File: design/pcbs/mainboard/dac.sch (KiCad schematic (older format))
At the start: 22 parts, among them U10 TPS7A49, U11 PCM1792A

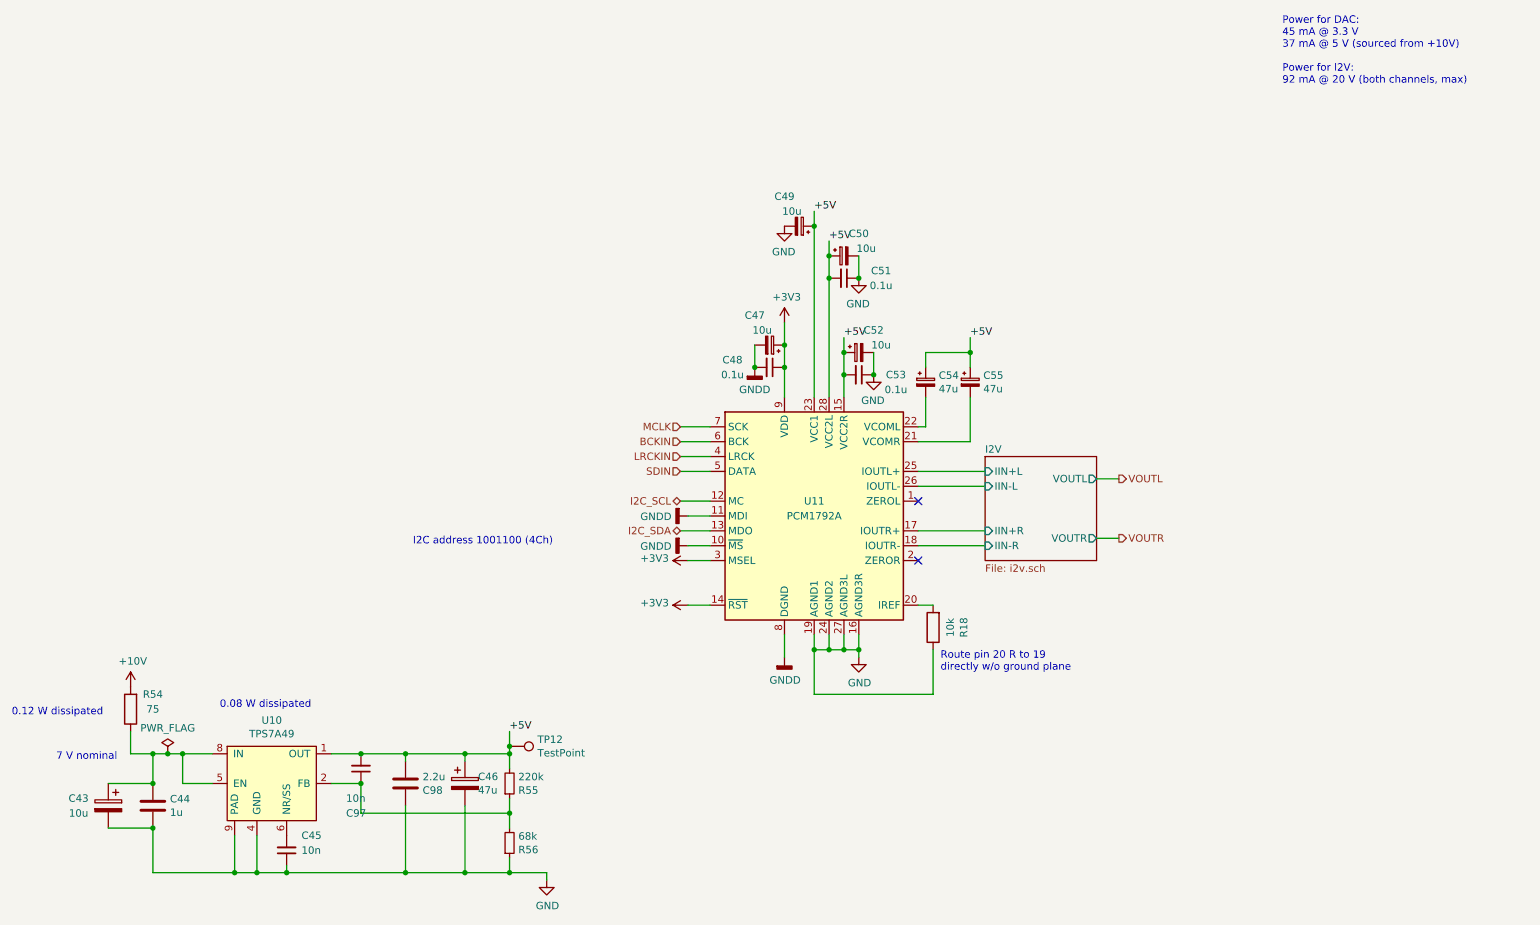
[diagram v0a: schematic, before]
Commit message: Renumbered footprints to follow board position.
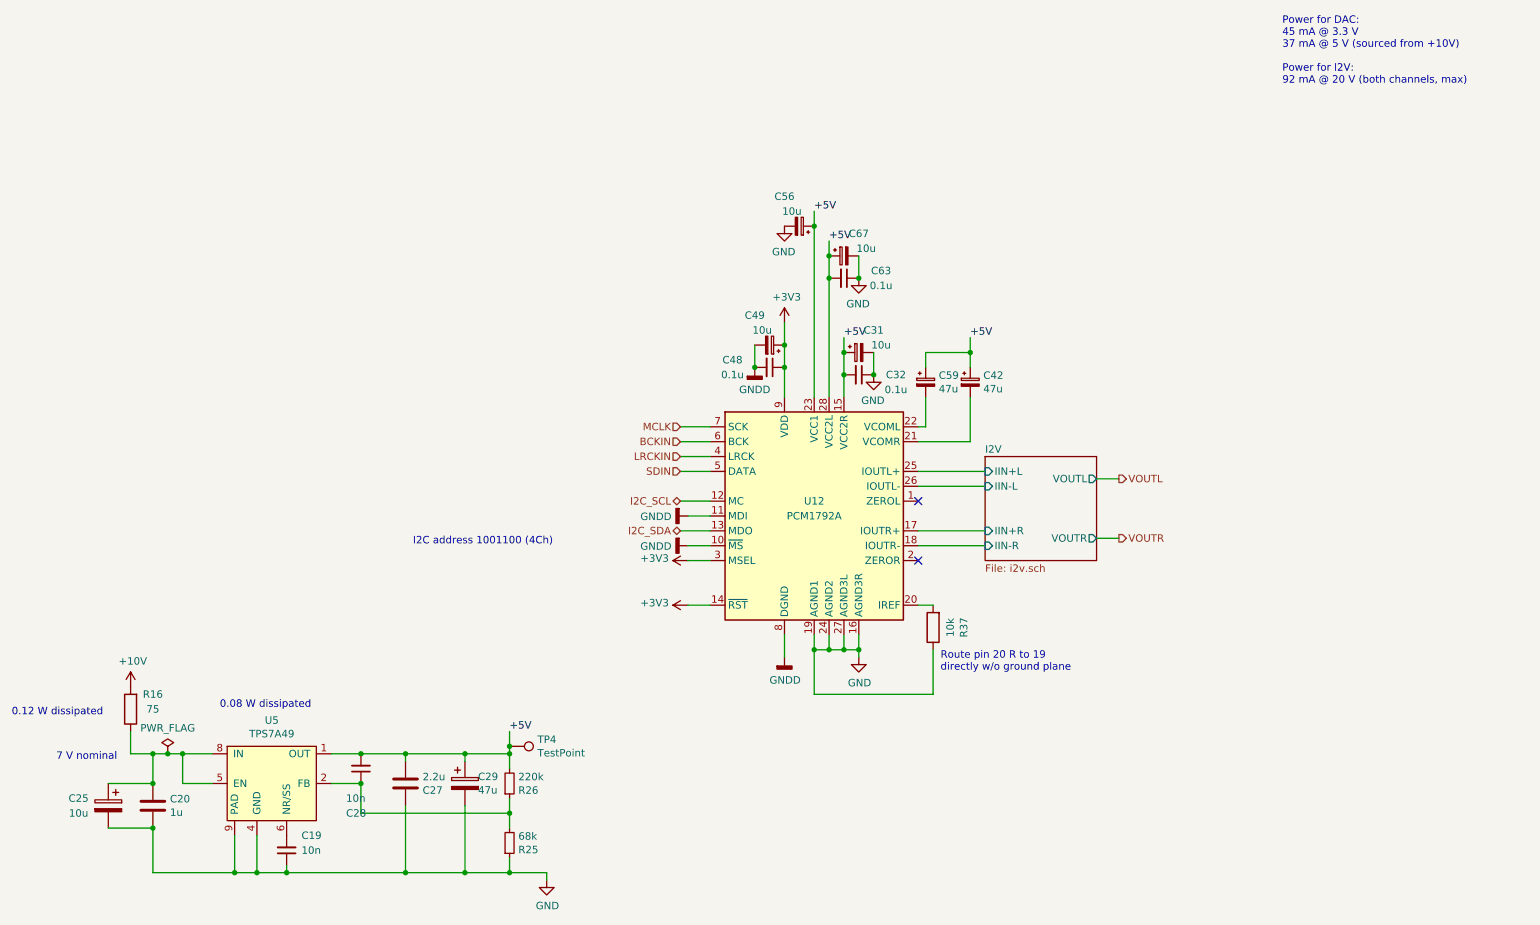
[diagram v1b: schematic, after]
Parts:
- renumbered C45 to C19, C44 to C20, C43 to C25, C98 to C27, C97 to C28, C46 to C29, C52 to C31, C53 to C32, C55 to C42, C47 to C49, C49 to C56, C54 to C59, C51 to C63, C50 to C67, R54 to R16, R56 to R25, R55 to R26, R18 to R37, TP12 to TP4, U11 to U12, U10 to U5
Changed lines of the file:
@@
 +5V
 $Comp
-L Device:C C44
+L Device:C C20
 U 1 1 5ECA0FE5
 P 2000 5900
-F 0 "C44" H 2115 5946 50  0000 L CNN
+F 0 "C20" H 2115 5946 50  0000 L CNN
 F 1 "1u" H 2115 5855 50  0000 L CNN
 F 2 "Capacitor_SMD:C_0805_2012Metric" H 2038 5750 50  0001 C CNN
@@
 	7250 4550 7150 4550
 $Comp
-L Device:R R18
+L Device:R R37
 U 1 1 5EC96EB0
 P 7250 4700
-F 0 "R18" V 7043 4700 50  0000 C CNN
+F 0 "R37" V 7043 4700 50  0000 C CNN
 F 1 "10k" V 7134 4700 50  0000 C CNN
 F 2 "Resistor_SMD:R_0402_1005Metric" V 7180 4700 50  0001 C CNN
@@
 	7200 3150 7200 3350
 $Comp
-L Audio:PCM1792A U11
+L Audio:PCM1792A U12
 U 1 1 5EC79C7B
 P 6450 3950
-F 0 "U11" H 6450 4050 50  0000 C CNN
+F 0 "U12" H 6450 4050 50  0000 C CNN
 F 1 "PCM1792A" H 6450 3950 50  0000 C CNN
 F 2 "Package_SO:SSOP-28_5.3x10.2mm_P0.65mm" H 6450 3950 50  0001 C CNN
@@
 Connection ~ 6650 3000
 $Comp
-L Device:C_Small C53
+L Device:C_Small C32
 U 1 1 5EC8EDB7
 P 6750 3000
-F 0 "C53" V 6750 3250 50  0000 C CNN
+F 0 "C32" V 6750 3250 50  0000 C CNN
 F 1 "0.1u" V 6850 3250 50  0000 C CNN
 F 2 "Capacitor_SMD:C_0603_1608Metric" H 6788 2850 50  0001 C CNN
@@
 Connection ~ 6550 2350
 $Comp
-L Device:C_Small C51
+L Device:C_Small C63
 U 1 1 5EC8BFA6
 P 6650 2350
-F 0 "C51" V 6600 2600 50  0000 C CNN
+F 0 "C63" V 6600 2600 50  0000 C CNN
 F 1 "0.1u" V 6700 2600 50  0000 C CNN
 F 2 "Capacitor_SMD:C_0603_1608Metric" H 6688 2200 50  0001 C CNN
@@
 $EndComp
 $Comp
-L Device:CP_Small C55
+L Device:CP_Small C42
 U 1 1 5EC776CB
 P 7500 3050
-F 0 "C55" H 7588 3096 50  0000 L CNN
+F 0 "C42" H 7588 3096 50  0000 L CNN
 F 1 "47u" H 7588 3005 50  0000 L CNN
 F 2 "Capacitor_THT:CP_Radial_D5.0mm_P2.00mm" H 7538 2900 50  0001 C CNN
@@
 $EndComp
 $Comp
-L Device:CP_Small C54
+L Device:CP_Small C59
 U 1 1 5EC768A9
 P 7200 3050
-F 0 "C54" H 7288 3096 50  0000 L CNN
+F 0 "C59" H 7288 3096 50  0000 L CNN
 F 1 "47u" H 7288 3005 50  0000 L CNN
 F 2 "Capacitor_THT:CP_Radial_D5.0mm_P2.00mm" H 7238 2900 50  0001 C CNN
@@
 P 6650 2200
 AR Path="/5EC77FFA/5ECF2F54" Ref="C?"  Part="1"
-AR Path="/5EC7811C/5ECF2F54" Ref="C50"  Part="1"
-F 0 "C50" V 6500 2100 50  0000 C CNN
+AR Path="/5EC7811C/5ECF2F54" Ref="C67"  Part="1"
+F 0 "C67" V 6500 2100 50  0000 C CNN
 F 1 "10u" V 6600 2050 50  0000 C CNN
 F 2 "Capacitor_Tantalum_SMD:CP_EIA-3216-18_Kemet-A" H 6688 2050 50  0001 C CNN
@@
 P 6350 2000
 AR Path="/5EC77FFA/5ECF477A" Ref="C?"  Part="1"
-AR Path="/5EC7811C/5ECF477A" Ref="C49"  Part="1"
-F 0 "C49" V 6550 1900 50  0000 C CNN
+AR Path="/5EC7811C/5ECF477A" Ref="C56"  Part="1"
+F 0 "C56" V 6550 1900 50  0000 C CNN
 F 1 "10u" V 6450 1950 50  0000 C CNN
 F 2 "Capacitor_Tantalum_SMD:CP_EIA-3216-18_Kemet-A" H 6388 1850 50  0001 C CNN
@@
 P 6150 2800
 AR Path="/5EC77FFA/5ECF5115" Ref="C?"  Part="1"
-AR Path="/5EC7811C/5ECF5115" Ref="C47"  Part="1"
-F 0 "C47" V 6350 2700 50  0000 C CNN
+AR Path="/5EC7811C/5ECF5115" Ref="C49"  Part="1"
+F 0 "C49" V 6350 2700 50  0000 C CNN
 F 1 "10u" V 6250 2750 50  0000 C CNN
 F 2 "Capacitor_Tantalum_SMD:CP_EIA-3216-18_Kemet-A" H 6188 2650 50  0001 C CNN
@@
 P 6750 2850
 AR Path="/5EC77FFA/5ECF5A07" Ref="C?"  Part="1"
-AR Path="/5EC7811C/5ECF5A07" Ref="C52"  Part="1"
-F 0 "C52" V 6600 2750 50  0000 C CNN
+AR Path="/5EC7811C/5ECF5A07" Ref="C31"  Part="1"
+F 0 "C31" V 6600 2750 50  0000 C CNN
 F 1 "10u" V 6700 2700 50  0000 C CNN
 F 2 "Capacitor_Tantalum_SMD:CP_EIA-3216-18_Kemet-A" H 6788 2700 50  0001 C CNN
@@
 P 1700 5900
 AR Path="/5EC77FFA/5ECD8C25" Ref="C?"  Part="1"
-AR Path="/5EC7811C/5ECD8C25" Ref="C43"  Part="1"
-F 0 "C43" H 1900 5950 50  0000 C CNN
+AR Path="/5EC7811C/5ECD8C25" Ref="C25"  Part="1"
+F 0 "C25" H 1900 5950 50  0000 C CNN
 F 1 "10u" H 1900 5850 50  0000 C CNN
 F 2 "Capacitor_Tantalum_SMD:CP_EIA-3216-18_Kemet-A" H 1738 5750 50  0001 C CNN
@@
 NoConn ~ 7150 4250
 $Comp
-L Connector:TestPoint TP12
+L Connector:TestPoint TP4
 U 1 1 5EE7E152
 P 4400 5500
-F 0 "TP12" V 4354 5688 50  0000 L CNN
+F 0 "TP4" V 4354 5688 50  0000 L CNN
 F 1 "TestPoint" V 4445 5688 50  0000 L CNN
 F 2 "TestPoint:TestPoint_THTPad_D3.0mm_Drill1.5mm" H 4600 5500 50  0001 C CNN
@@
 	6250 4750 6250 4900
 $Comp
-L Device:R R54
+L Device:R R16
 U 1 1 5EE0ACD0
 P 1850 5250
-F 0 "R54" H 1700 5150 50  0000 C CNN
+F 0 "R16" H 1700 5150 50  0000 C CNN
 F 1 "75" H 1700 5250 50  0000 C CNN
 F 2 "Resistor_SMD:R_1206_3216Metric" V 1780 5250 50  0001 C CNN
@@
 P 3400 5650
 AR Path="/5EC7824B/5EE227BA" Ref="C?"  Part="1"
-AR Path="/5EC7811C/5EE227BA" Ref="C97"  Part="1"
-F 0 "C97" H 3300 5950 50  0000 L CNN
+AR Path="/5EC7811C/5EE227BA" Ref="C28"  Part="1"
+F 0 "C28" H 3300 5950 50  0000 L CNN
 F 1 "10n" H 3300 5850 50  0000 L CNN
 F 2 "Capacitor_SMD:C_0603_1608Metric" H 3438 5500 50  0001 C CNN
@@
 P 2900 6200
 AR Path="/5EC7824B/5EE227C6" Ref="C?"  Part="1"
-AR Path="/5EC7811C/5EE227C6" Ref="C45"  Part="1"
-F 0 "C45" H 3000 6100 50  0000 L CNN
+AR Path="/5EC7811C/5EE227C6" Ref="C19"  Part="1"
+F 0 "C19" H 3000 6100 50  0000 L CNN
 F 1 "10n" H 3000 6200 50  0000 L CNN
 F 2 "Capacitor_SMD:C_0603_1608Metric" H 2938 6050 50  0001 C CNN
@@
 P 4400 5750
 AR Path="/5EC7824B/5EE227CF" Ref="R?"  Part="1"
-AR Path="/5EC7811C/5EE227CF" Ref="R55"  Part="1"
-F 0 "R55" H 4459 5796 50  0000 L CNN
+AR Path="/5EC7811C/5EE227CF" Ref="R26"  Part="1"
+F 0 "R26" H 4459 5796 50  0000 L CNN
 F 1 "220k" H 4459 5705 50  0000 L CNN
 F 2 "Resistor_SMD:R_0402_1005Metric" H 4400 5750 50  0001 C CNN
@@
 P 4400 6150
 AR Path="/5EC7824B/5EE227ED" Ref="R?"  Part="1"
-AR Path="/5EC7811C/5EE227ED" Ref="R56"  Part="1"
-F 0 "R56" H 4459 6196 50  0000 L CNN
+AR Path="/5EC7811C/5EE227ED" Ref="R25"  Part="1"
+F 0 "R25" H 4459 6196 50  0000 L CNN
 F 1 "68k" H 4459 6105 50  0000 L CNN
 F 2 "Resistor_SMD:R_0402_1005Metric" H 4400 6150 50  0001 C CNN
@@
 P 2800 5750
 AR Path="/5EC7824B/5EE227AD" Ref="U?"  Part="1"
-AR Path="/5EC7811C/5EE227AD" Ref="U10"  Part="1"
-F 0 "U10" H 2800 6175 50  0000 C CNN
+AR Path="/5EC7811C/5EE227AD" Ref="U5"  Part="1"
+F 0 "U5" H 2800 6175 50  0000 C CNN
 F 1 "TPS7A49" H 2800 6084 50  0000 C CNN
 F 2 "Package_SO:MSOP-8-1EP_3x3mm_P0.65mm_EP1.68x1.88mm_ThermalVias" H 2750 5750 50  0001 C CNN
@@
 	1850 5400 1850 5550
 $Comp
-L Device:CP C46
+L Device:CP C29
 U 1 1 5EDC1BA1
 P 4100 5750
-F 0 "C46" H 4188 5796 50  0000 L CNN
+F 0 "C29" H 4188 5796 50  0000 L CNN
 F 1 "47u" H 4188 5705 50  0000 L CNN
 F 2 "Capacitor_THT:CP_Radial_D5.0mm_P2.00mm" H 4138 5600 50  0001 C CNN
@@
 P 3700 5750
 AR Path="/5EC7824B/5EE22817" Ref="C?"  Part="1"
-AR Path="/5EC7811C/5EE22817" Ref="C98"  Part="1"
-F 0 "C98" H 3815 5796 50  0000 L CNN
+AR Path="/5EC7811C/5EE22817" Ref="C27"  Part="1"
+F 0 "C27" H 3815 5796 50  0000 L CNN
 F 1 "2.2u" H 3815 5705 50  0000 L CNN
 F 2 "Capacitor_SMD:C_1206_3216Metric" H 3738 5600 50  0001 C CNN

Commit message: Fixed title blocks. Added fab outputs.
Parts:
- U5: LCSC (none) -> C16430
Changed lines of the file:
@@
 encoding utf-8
 Sheet 6 10
-Title ""
-Date ""
-Rev ""
-Comp ""
-Comment1 ""
-Comment2 ""
+Title "DAC1 Main board"
+Date "2020-06-27"
+Rev "1.0.0"
+Comp "© Mark Pinese 2020"
+Comment1 "To view a copy of this license, visit https://creativecommons.org/licenses/by/4.0"
+Comment2 "This work is licensed under CC BY 4.0."
 Comment3 ""
 Comment4 ""
@@
 F 4 "296-27751-1-ND" H 2800 5750 50  0001 C CNN "DigiKey"
 F 5 "Yes" H 2800 5750 50  0001 C CNN "Done"
+F 6 "C16430" H 2800 5750 50  0001 C CNN "LCSC"
 	1    2800 5750
 	1    0    0    -1

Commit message: Misc updates
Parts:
- added FB3: Ferrite_Bead_Small, Resistor_SMD:R_0603_1608Metric_Pad1.05x0.95mm_HandSolder, symbol Device:Ferrite_Bead_Small
- C42, C59: footprint Capacitor_THT:CP_Radial_D5.0mm_P2.00mm -> Capacitor_THT:CP_Radial_D6.3mm_P2.50mm; DigiKey 732-9306-1-ND -> 493-15014-ND; Function Noise reduction -> (none)
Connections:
- net +3V3: now also FB3.1; no longer U12.9 (VDD)
- net GND: now also C48.2, C49.2, U12.8 (DGND)
- net GNDD: no longer C48.2, C49.2, U12.8 (DGND)
- new net: FB3.2, U12.9 (VDD)
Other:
- moved on the sheet: C48, C49
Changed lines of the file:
@@
 	0    1    1    0
 $EndComp
-Connection ~ 6050 2950
-Wire Wire Line
-	6050 2950 6050 2800
-Wire Wire Line
-	6250 2950 6250 3150
-Connection ~ 6250 2950
+Wire Wire Line
+	6050 2750 6050 2600
 Connection ~ 6750 2350
 Wire Wire Line
@@
 $EndComp
 $Comp
-L Device:CP_Small C42
-U 1 1 5EC776CB
-P 7500 3050
-F 0 "C42" H 7588 3096 50  0000 L CNN
-F 1 "47u" H 7588 3005 50  0000 L CNN
-F 2 "Capacitor_THT:CP_Radial_D5.0mm_P2.00mm" H 7538 2900 50  0001 C CNN
-F 3 "https://katalog.we-online.de/pbs/datasheet/860240272001.pdf" H 7500 3050 50  0001 C CNN
-F 4 "<= 5V" H 7500 3050 50  0001 C CNN "Vbias"
-F 5 "Noise reduction" H 7500 3050 50  0001 C CNN "Function"
-F 6 "732-9306-1-ND" H 7500 3050 50  0001 C CNN "DigiKey"
-F 7 "Yes" H 7500 3050 50  0001 C CNN "Done"
-	1    7500 3050
-	1    0    0    -1
-$EndComp
-$Comp
 L Device:CP_Small C59
 U 1 1 5EC768A9
@@
 F 0 "C59" H 7288 3096 50  0000 L CNN
 F 1 "47u" H 7288 3005 50  0000 L CNN
-F 2 "Capacitor_THT:CP_Radial_D5.0mm_P2.00mm" H 7238 2900 50  0001 C CNN
-F 3 "https://katalog.we-online.de/pbs/datasheet/860240272001.pdf" H 7200 3050 50  0001 C CNN
+F 2 "Capacitor_THT:CP_Radial_D6.3mm_P2.50mm" H 7238 2900 50  0001 C CNN
+F 3 "" H 7200 3050 50  0001 C CNN
 F 4 "<= 5V" H 7200 3050 50  0001 C CNN "Vbias"
-F 5 "Noise reduction" H 7200 3050 50  0001 C CNN "Function"
-F 6 "732-9306-1-ND" H 7200 3050 50  0001 C CNN "DigiKey"
+F 5 "" H 7200 3050 50  0001 C CNN "Function"
+F 6 "493-15014-ND" H 7200 3050 50  0001 C CNN "DigiKey"
 F 7 "Yes" H 7200 3050 50  0001 C CNN "Done"
 	1    7200 3050
@@
 $EndComp
 $Comp
-L power:GNDD #PWR069
-U 1 1 5EC7256D
-P 6050 2950
-F 0 "#PWR069" H 6050 2700 50  0001 C CNN
-F 1 "GNDD" H 6050 2800 50  0000 C CNN
-F 2 "" H 6050 2950 50  0001 C CNN
-F 3 "" H 6050 2950 50  0001 C CNN
-	1    6050 2950
-	1    0    0    -1
-$EndComp
-$Comp
 L Device:C_Small C48
 U 1 1 5EC6F4C3
-P 6150 2950
-F 0 "C48" V 6100 2700 50  0000 C CNN
-F 1 "0.1u" V 6200 2700 50  0000 C CNN
-F 2 "Capacitor_SMD:C_0603_1608Metric" H 6188 2800 50  0001 C CNN
-F 3 "https://datasheet.lcsc.com/szlcsc/YAGEO-CC0603KRX7R9BB104_C14663.pdf" H 6150 2950 50  0001 C CNN
-F 4 "C14663" H 6150 2950 50  0001 C CNN "LCSC"
-F 5 "3.3" V 6150 2950 50  0001 C CNN "Vbias"
-F 6 "Decoupling" H 6150 2950 50  0001 C CNN "Function"
-F 7 "Yes" H 6150 2950 50  0001 C CNN "Done"
-	1    6150 2950
+P 6150 2750
+F 0 "C48" V 6100 2500 50  0000 C CNN
+F 1 "0.1u" V 6200 2500 50  0000 C CNN
+F 2 "Capacitor_SMD:C_0603_1608Metric" H 6188 2600 50  0001 C CNN
+F 3 "https://datasheet.lcsc.com/szlcsc/YAGEO-CC0603KRX7R9BB104_C14663.pdf" H 6150 2750 50  0001 C CNN
+F 4 "C14663" H 6150 2750 50  0001 C CNN "LCSC"
+F 5 "3.3" V 6150 2750 50  0001 C CNN "Vbias"
+F 6 "Decoupling" H 6150 2750 50  0001 C CNN "Function"
+F 7 "Yes" H 6150 2750 50  0001 C CNN "Done"
+	1    6150 2750
 	0    1    1    0
 $EndComp
@@
 L power:+3V3 #PWR071
 U 1 1 5EC6E821
-P 6250 2650
-F 0 "#PWR071" H 6250 2500 50  0001 C CNN
-F 1 "+3V3" H 6265 2823 50  0000 C CNN
-F 2 "" H 6250 2650 50  0001 C CNN
-F 3 "" H 6250 2650 50  0001 C CNN
-	1    6250 2650
+P 6250 2450
+F 0 "#PWR071" H 6250 2300 50  0001 C CNN
+F 1 "+3V3" H 6265 2623 50  0000 C CNN
+F 2 "" H 6250 2450 50  0001 C CNN
+F 3 "" H 6250 2450 50  0001 C CNN
+	1    6250 2450
 	1    0    0    -1
 $EndComp
@@
 	0    1    1    0
 $EndComp
-$Comp
-L power:GNDD #PWR072
-U 1 1 5EC6BB00
-P 6250 4900
-F 0 "#PWR072" H 6250 4650 50  0001 C CNN
-F 1 "GNDD" H 6254 4745 50  0000 C CNN
-F 2 "" H 6250 4900 50  0001 C CNN
-F 3 "" H 6250 4900 50  0001 C CNN
-	1    6250 4900
-	1    0    0    -1
-$EndComp
 Wire Wire Line
 	5600 4250 5750 4250
@@
 	0    -1   -1   0
 $EndComp
-Wire Wire Line
-	5550 3350 5750 3350
-Wire Wire Line
-	5750 3650 5550 3650
-Wire Wire Line
-	5550 3550 5750 3550
-Wire Wire Line
-	5550 3450 5750 3450
-Text HLabel 5550 3350 0    50   Input ~ 0
-MCLK
-Text HLabel 5550 3550 0    50   Input ~ 0
-LRCKIN
-Text HLabel 5550 3450 0    50   Input ~ 0
-BCKIN
-Text HLabel 5550 3650 0    50   Input ~ 0
-SDIN
 Text HLabel 5550 4050 0    50   BiDi ~ 0
 I2C_SDA
@@
 	6450 1900 6450 2000
 Wire Wire Line
-	6250 2650 6250 2800
+	6250 2450 6250 2600
 $Comp
 L Device:CP_Small C?
@@
 L Device:CP_Small C?
 U 1 1 5ECF5115
-P 6150 2800
+P 6150 2600
 AR Path="/5EC77FFA/5ECF5115" Ref="C?"  Part="1"
 AR Path="/5EC7811C/5ECF5115" Ref="C49"  Part="1"
-F 0 "C49" V 6350 2700 50  0000 C CNN
-F 1 "10u" V 6250 2750 50  0000 C CNN
-F 2 "Capacitor_Tantalum_SMD:CP_EIA-3216-18_Kemet-A" H 6188 2650 50  0001 C CNN
-F 3 "https://datasheet.lcsc.com/szlcsc/AVX-TAJA106K016RNJ_C7171.pdf" H 6150 2800 50  0001 C CNN
-F 4 "3.3" V 6150 2800 50  0001 C CNN "Vbias"
-F 5 "Decoupling" H 6150 2800 50  0001 C CNN "Function"
-F 6 "" V 6150 2800 50  0001 C CNN "DigiKey"
-F 7 "C7171" H 6150 2800 50  0001 C CNN "LCSC"
-F 8 "Yes" H 6150 2800 50  0001 C CNN "Done"
-	1    6150 2800
+F 0 "C49" V 6350 2500 50  0000 C CNN
+F 1 "10u" V 6250 2550 50  0000 C CNN
+F 2 "Capacitor_Tantalum_SMD:CP_EIA-3216-18_Kemet-A" H 6188 2450 50  0001 C CNN
+F 3 "https://datasheet.lcsc.com/szlcsc/AVX-TAJA106K016RNJ_C7171.pdf" H 6150 2600 50  0001 C CNN
+F 4 "3.3" V 6150 2600 50  0001 C CNN "Vbias"
+F 5 "Decoupling" H 6150 2600 50  0001 C CNN "Function"
+F 6 "" V 6150 2600 50  0001 C CNN "DigiKey"
+F 7 "C7171" H 6150 2600 50  0001 C CNN "LCSC"
+F 8 "Yes" H 6150 2600 50  0001 C CNN "Done"
+	1    6150 2600
 	0    1    -1   0
 $EndComp
-Connection ~ 6250 2800
-Wire Wire Line
-	6250 2800 6250 2950
+Connection ~ 6250 2600
+Wire Wire Line
+	6250 2600 6250 2750
 Wire Wire Line
 	6650 2750 6650 2850
@@
 $EndComp
 Wire Wire Line
-	6250 4750 6250 4900
+	6250 4750 6250 4850
 $Comp
 L Device:R R16
@@
 Wire Wire Line
 	2100 5550 2200 5550
+Text HLabel 5550 3350 0    50   Input ~ 0
+MCLK
+Wire Wire Line
+	5550 3350 5750 3350
+Wire Wire Line
+	6450 4850 6250 4850
+$Comp
+L power:GND #PWR032
+U 1 1 5EFF5170
+P 6050 2750
+F 0 "#PWR032" H 6050 2500 50  0001 C CNN
+F 1 "GND" H 6055 2577 50  0000 C CNN
+F 2 "" H 6050 2750 50  0001 C CNN
+F 3 "" H 6050 2750 50  0001 C CNN
+	1    6050 2750
+	1    0    0    -1
+$EndComp
+Connection ~ 6050 2750
+$Comp
+L Device:Ferrite_Bead_Small FB3
+U 1 1 5EFFB866
+P 6250 2950
+F 0 "FB3" H 6050 2900 50  0000 L CNN
+F 1 "Ferrite_Bead_Small" H 6350 2905 50  0001 L CNN
+F 2 "Resistor_SMD:R_0603_1608Metric_Pad1.05x0.95mm_HandSolder" V 6180 2950 50  0001 C CNN
+F 3 "~" H 6250 2950 50  0001 C CNN
+	1    6250 2950
+	1    0    0    -1
+$EndComp
+Wire Wire Line
+	6250 2850 6250 2750
+Connection ~ 6250 2750
+Wire Wire Line
+	6250 3050 6250 3150
+Wire Wire Line
+	5750 3650 5550 3650
+Wire Wire Line
+	5550 3550 5750 3550
+Wire Wire Line
+	5550 3450 5750 3450
+Text HLabel 5550 3550 0    50   Input ~ 0
+LRCKIN
+Text HLabel 5550 3450 0    50   Input ~ 0
+BCKIN
+Text HLabel 5550 3650 0    50   Input ~ 0
+SDIN
+$Comp
+L Device:CP_Small C42
+U 1 1 5EC776CB
+P 7500 3050
+F 0 "C42" H 7588 3096 50  0000 L CNN
+F 1 "47u" H 7588 3005 50  0000 L CNN
+F 2 "Capacitor_THT:CP_Radial_D6.3mm_P2.50mm" H 7538 2900 50  0001 C CNN
+F 3 "" H 7500 3050 50  0001 C CNN
+F 4 "<= 5V" H 7500 3050 50  0001 C CNN "Vbias"
+F 5 "" H 7500 3050 50  0001 C CNN "Function"
+F 6 "493-15014-ND" H 7500 3050 50  0001 C CNN "DigiKey"
+F 7 "Yes" H 7500 3050 50  0001 C CNN "Done"
+	1    7500 3050
+	1    0    0    -1
+$EndComp
 $EndSCHEMATC
